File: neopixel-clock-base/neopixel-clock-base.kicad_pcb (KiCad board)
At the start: 2 copper layers, 27.7 x 68.3 mm, 14 parts, among them J0 Power, J1(H) Neopixel_12, J2(M) Neopixel_24, J3(S) Neopixel_60, U0 Chronodot

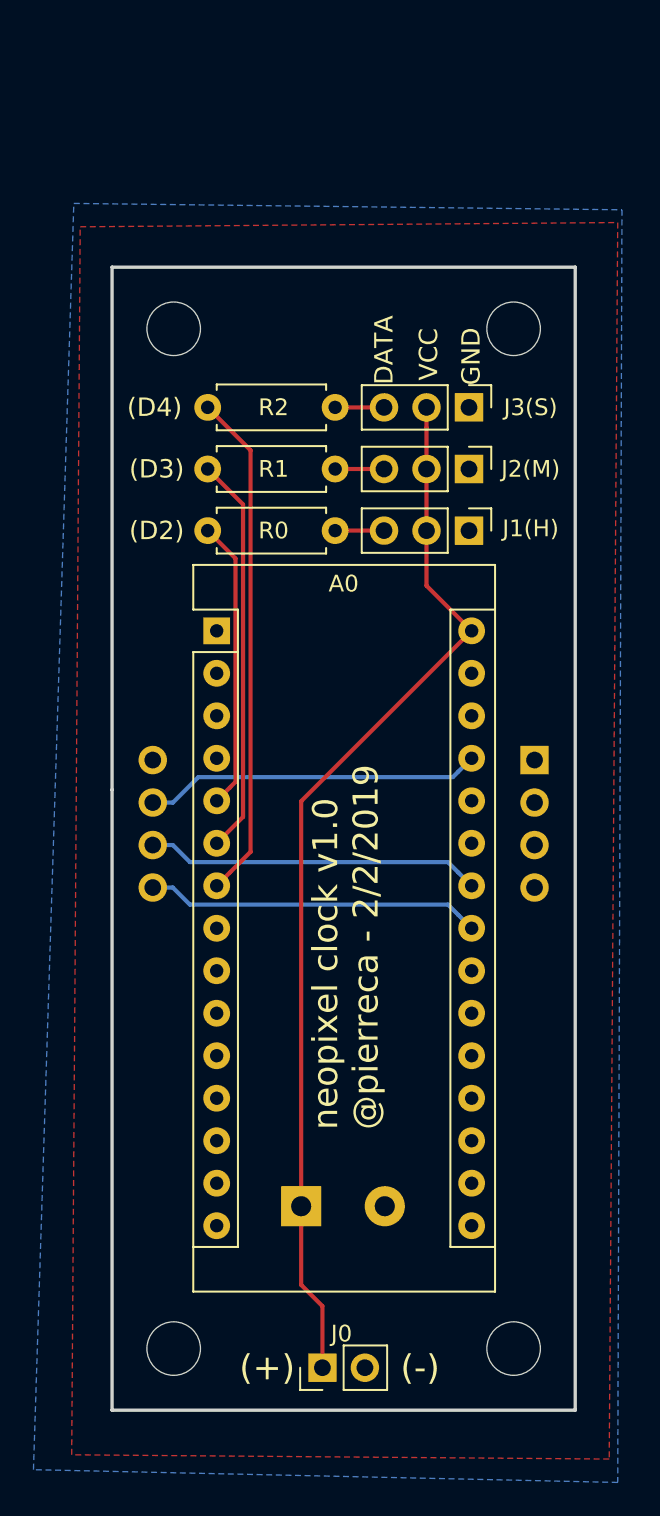
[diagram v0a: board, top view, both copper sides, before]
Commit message: add 2 pushbuttons to neopixel clock pcb design
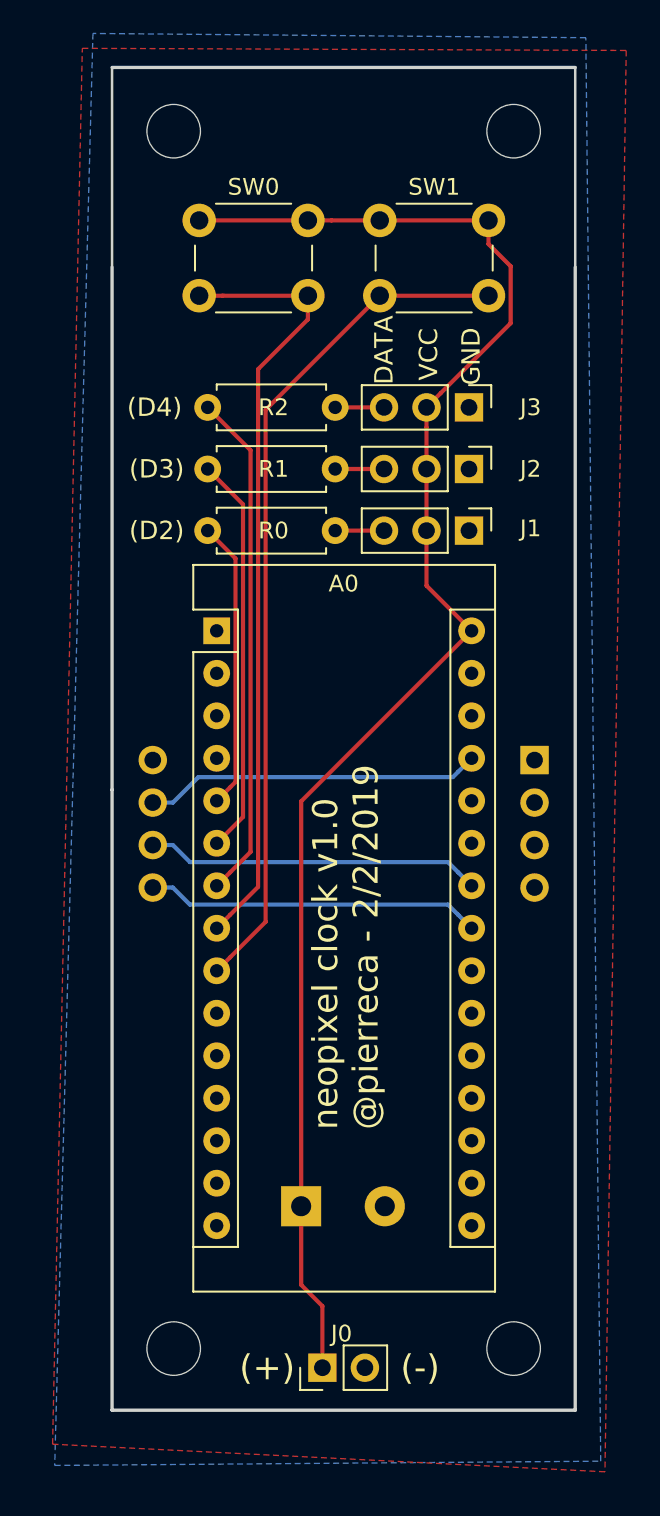
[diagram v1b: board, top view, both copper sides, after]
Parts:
- added SW0: SW_Push, Button_Switch_THT:SW_PUSH_6mm, F.Cu at (135.1, 78.5)
- added SW1: SW_Push, Button_Switch_THT:SW_PUSH_6mm, F.Cu at (145.9, 78.5)
- moved ? 11.8 mm to (133.6, 73.2)
- moved ? 11.8 mm to (153.9, 73.2)
- renumbered J1(H) to J1, J2(M) to J2, J3(S) to J3
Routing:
- net Net-(A0-Pad9): track 0.00 -> 50.9 mm
- net Net-(A0-Pad8): track 0.00 -> 46.6 mm
- net Net-(A0-Pad30): track 63.3 -> 94.4 mm
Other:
- board size 27.7 x 68.3 mm -> 27.7 x 80.3 mm
